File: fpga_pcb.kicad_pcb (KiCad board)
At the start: 2 copper layers, 254 parts, among them J1 USB_B_Mini, J10 Conn_02x08_Odd_Even, J11 Conn_02x08_Odd_Even, J12 5VIN, J13 Conn_01x10, J14 RJ45_Halo_HFJ11-x2450E-LxxRL, J2 Conn_01x06, J3 Conn_01x06, J4 Conn_01x06, J5 Conn_01x06, J6 Conn_01x06, J7 Conn_01x06, J8 Conn_01x06, J9 Conn_01x06, SW1 SW_Push, SW2 SW_Push, U10 LAN8720A, U2 23AA02M-IST, U3 TPS62A02APDDC, U4 TLV75733PDBV, U5 TPS2116DRL, U6 93AAxxBT-xOT, U7 USBLC6-2SC6, U8 FT4232H, U9 ADC1283, Y1 ECS-2520MV-500-xx, Y2 Crystal_GND24

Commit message: More layout
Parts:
- D7: footprint Diode_SMD:D_SOD-123 -> Diode_SMD:D_SMA
- D8: footprint Diode_SMD:D_SOD-923 -> Diode_SMD:D_SMA
- moved J9 302.0 mm to (258.0, 118.0), turned to -90 degrees
- moved J8 301.8 mm to (258.0, 106.0), turned to -90 degrees
- moved J7 301.7 mm to (258.0, 94.0), turned to -90 degrees
- moved J6 301.7 mm to (258.0, 82.0), turned to -90 degrees
- moved J5 291.2 mm to (244.0, 118.0), turned to -90 degrees
- moved J4 290.5 mm to (244.0, 106.0), turned to -90 degrees
- moved J3 290.0 mm to (244.0, 94.0), turned to -90 degrees
- moved J2 289.4 mm to (244.0, 82.0), turned to -90 degrees
- moved C54 289.0 mm to (253.5, 103.5), turned to -90 degrees
- moved C52 288.7 mm to (253.5, 79.5), turned to -90 degrees
- moved C53 288.7 mm to (253.5, 91.5), turned to -90 degrees
- moved C55 287.5 mm to (253.5, 115.5), turned to -90 degrees
- moved R61 281.4 mm to (254.0, 99.0)
- moved R62 281.3 mm to (254.0, 100.5), turned to 180 degrees
- moved R59 281.2 mm to (254.0, 87.0)
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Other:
- copper layers 2 -> 4
- board text added: "3V3 GND SCK D0 WS SEL"
- board text added: "3V3 GND SCK D1 WS SEL"
- board text added: "3V3 GND SCK D2 WS SEL"
- board text added: "3V3 GND SCK D3 WS SEL"

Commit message: More layout
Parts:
- moved J9 226.6 mm to (49.5, 206.8), turned to 180 degrees
- moved R66 224.8 mm to (43.0, 202.6), turned to 90 degrees
- moved R65 223.9 mm to (44.5, 202.6), turned to -90 degrees
- moved J8 220.8 mm to (61.5, 206.8), turned to 180 degrees
- moved C55 219.4 mm to (52.0, 202.2), turned to 180 degrees
- moved R64 218.5 mm to (55.0, 202.8), turned to 90 degrees
- moved R63 217.8 mm to (56.5, 202.8), turned to -90 degrees
- moved C2 217.6 mm to (55.2, 185.0), turned to -90 degrees
- moved J7 216.2 mm to (73.5, 206.8), turned to 180 degrees
- moved C1 214.7 mm to (74.5, 160.5), turned to 180 degrees
- moved C3 214.4 mm to (53.2, 185.0), turned to -90 degrees
- moved C54 213.7 mm to (64.0, 202.2), turned to 180 degrees
- moved C24 213.5 mm to (74.2, 174.8)
- moved R62 213.1 mm to (67.0, 202.8), turned to 90 degrees
- moved J6 212.9 mm to (85.5, 206.8), turned to 180 degrees
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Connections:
- J12 pad 1: Net-(D7-K) -> GND
- J12 pad 2: GND -> Net-(D7-K)
- U1 pad 2: /FPGA/UART.TX -> /FPGA/I2S.SCK
- U1 pad 29: /FPGA/BB0 -> /FPGA/USR_LED_R
- U1 pad 3: /FPGA/UART.RX -> /FPGA/I2S.WS
- U1 pad 30: /FPGA/BB1 -> /FPGA/USR_LED_G
- U1 pad 32: /FPGA/BB2 -> /FPGA/USR_LED_B
- U1 pad 33: /FPGA/BB3 -> /ADC/ADC_SPI.CS
- U1 pad 35: /FPGA/BB4 -> /ADC/ADC_SPI.SCLK
- U1 pad 36: /FPGA/BB5 -> /ADC/ADC_SPI.DIN
- U1 pad 37: /FPGA/BB6 -> /ADC/ADC_SPI.DOUT
- U1 pad 38: /FPGA/BB7 -> /FPGA/RAM.SIO0
- U1 pad 4: /FPGA/USR_LED_R -> /FPGA/I2S.DATA0
- U1 pad 40: /FPGA/I2S.SCK -> /FPGA/RAM.SCK
- U1 pad 41: /FPGA/I2S.WS -> /FPGA/RAM.SIO3
- U1 pad 43: /FPGA/I2S.DATA0 -> /FPGA/RAM.CS
- U1 pad 44: /FPGA/I2S.DATA1 -> /FPGA/RAM.SIO1
- U1 pad 46: /FPGA/I2S.DATA2 -> /FPGA/RAM.SIO2
- U1 pad 47: /FPGA/I2S.DATA3 -> /FPGA/GPIO0
- U1 pad 48: /FPGA/GPIO0 -> /FPGA/GPIO1
- U1 pad 49: /FPGA/GPIO1 -> /FPGA/GPIO2
- U1 pad 5: /FPGA/USR_LED_G -> /FPGA/I2S.DATA1
- U1 pad 51: /FPGA/GPIO2 -> /FPGA/GPIO3
- U1 pad 52: /FPGA/GPIO3 -> /FPGA/GPIO4
- U1 pad 54: /FPGA/GPIO4 -> /FPGA/GPIO5
- U1 pad 55: /FPGA/GPIO5 -> /FPGA/GPIO6
- U1 pad 56: /FPGA/GPIO6 -> /FPGA/GPIO7
- U1 pad 62: /FPGA/GPIO7 -> /FPGA/BB0
- U1 pad 63: /ADC/ADC_SPI.CS -> /FPGA/BB1
- U1 pad 65: /ADC/ADC_SPI.SCLK -> /FPGA/BB2
- U1 pad 66: /ADC/ADC_SPI.DIN -> /FPGA/BB3
- U1 pad 67: /ADC/ADC_SPI.DOUT -> /FPGA/BB4
- U1 pad 68: /FPGA/RAM.CS -> /FPGA/BB5
- U1 pad 7: /FPGA/CLK -> /FPGA/I2S.DATA2
- U1 pad 71: /FPGA/RAM.SCK -> /FPGA/BB6
- U1 pad 73: /FPGA/RAM.SIO0 -> /FPGA/BB7
- U1 pad 74: /FPGA/RAM.SIO1 -> /FPGA/UART.TX
- U1 pad 77: /FPGA/RAM.SIO2 -> /FPGA/UART.RX
- U1 pad 78: /FPGA/RAM.SIO3 -> /Ethernet/RMII.TXD0
- U1 pad 79: /Ethernet/RMII.TXD0 -> /Ethernet/RMII.TXD1
- U1 pad 80: /Ethernet/RMII.TXD1 -> /Ethernet/RMII.TXEN
- U1 pad 85: /Ethernet/RMII.TXEN -> /Ethernet/RMII.RXD0
- U1 pad 86: /Ethernet/RMII.RXD0 -> /FPGA/CLK
- U1 pad 9: /FPGA/USR_LED_B -> /FPGA/I2S.DATA3
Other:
- board outline added: 100 x 65 mm
- board text added: "3V3 GND IO0 IO1 IO2 IO3 IO4 IO5 IO6 IO7"
- board text added: "GND 3V3 HOLD RSTN CS MISO MOSI SCLK"
- board text added: "GND 3V3 TMS TDO TDI TCK RX TX"

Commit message: Initial layout
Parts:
- moved R17 209.8 mm to (84.0, 160.2), turned to 90 degrees
- moved R8 208.5 mm to (51.8, 185.5), turned to 90 degrees
- moved R12 205.4 mm to (59.8, 185.5), turned to 90 degrees
- moved R15 201.8 mm to (87.0, 160.2), turned to -90 degrees
- moved D1 201.1 mm to (80.2, 157.2), turned to -90 degrees
- moved R21 199.1 mm to (78.8, 160.2), turned to 90 degrees
- moved R16 199.1 mm to (85.5, 160.2), turned to -90 degrees
- moved D2 198.4 mm to (78.8, 157.2), turned to -90 degrees
- moved R14 198.2 mm to (80.2, 160.2), turned to 90 degrees
- moved R25 197.2 mm to (66.0, 180.2)
- moved R7 193.5 mm to (58.8, 158.0), turned to 90 degrees
- moved R18 192.5 mm to (60.2, 161.5), turned to -90 degrees
- moved R19 191.6 mm to (61.8, 161.5), turned to -90 degrees
- moved R27 191.0 mm to (37.8, 176.8), turned to 180 degrees
- moved R10 190.3 mm to (65.2, 155.0), turned to 180 degrees
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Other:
- board text added: "A7 A6 A5 A4 A3 A2 A1 A0"

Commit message: Routing done
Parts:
- removed JP1: SolderJumper_2_Bridged, Jumper:SolderJumper-2_P1.3mm_Bridged_RoundedPad1.0x1.5mm
- removed JP2: SolderJumper_2_Open, Jumper:SolderJumper-2_P1.3mm_Open_RoundedPad1.0x1.5mm
- removed TP15, TP16, TP17, TP19, TP20, TP21, TP22, TP23, TP24, TP25, TP26, TP27, TP28, TP35, TP36, TP37, TP38, TP39, TP4, TP40, TP41, TP42, TP43, TP44, TP45, TP5, TP6, TP7, TP8, TP9: TestPoint, TestPoint:TestPoint_Pad_D1.0mm
- added NT1: NetTie_2, NetTie:NetTie-2_SMD_Pad0.5mm, F.Cu at (31.7, 195.4)
- added R45: 5.1k, Resistor_SMD:R_0603_1608Metric, F.Cu at (10.2, 156.5)
- added R46: 5.1k, Resistor_SMD:R_0603_1608Metric, F.Cu at (10.2, 163.5)
- J1: value USB_B_Mini -> USB_C_Receptacle_USB2.0_16P; footprint Connector_USB:USB_Mini-B_Wuerth_65100516121_Horizontal -> Connector_USB:USB_C_Receptacle_GCT_USB4105-xx-A_16P_TopMnt_Horizontal
- moved TP29 121.0 mm to (85.5, 187.5)
- moved TP2 119.0 mm to (73.6, 182.5)
- moved TP33 115.3 mm to (83.5, 187.5)
- moved TP1 113.3 mm to (80.2, 152.1)
- moved TP30 110.2 mm to (73.0, 187.8)
- moved TP32 100.7 mm to (61.5, 187.5)
- moved TP3 95.2 mm to (34.2, 195.2)
- moved TP31 93.3 mm to (46.5, 185.5)
- moved TP34 92.0 mm to (48.8, 187.5)
- moved TP10 72.0 mm to (24.2, 181.0)
- moved TP11 67.6 mm to (33.2, 169.8)
- moved TP12 63.3 mm to (9.50, 168.8)
- moved TP13 59.1 mm to (24.0, 166.5)
- moved TP18 50.2 mm to (40.2, 154.0)
- moved TP14 38.9 mm to (24.8, 148.0)
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- renumbered R45 to R47, R46 to R48, R47 to R49, R48 to R50, R49 to R89, R50 to R90
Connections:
- F1 pad 2: Net-(J1-VBUS) -> Net-(F1-Pad2)
- J1 pad SH: Net-(J1-Shield) -> GND
- U1 pad 100: /Ethernet/RMII.INT -> /Ethernet/RMII.RXD1
- U1 pad 4: /FPGA/I2S.DATA0 -> /FPGA/I2S.DATA3
- U1 pad 5: /FPGA/I2S.DATA1 -> /FPGA/I2S.DATA2
- U1 pad 7: /FPGA/I2S.DATA2 -> /FPGA/I2S.DATA1
- U1 pad 74: /FPGA/UART.TX -> /FPGA/UART.RX
- U1 pad 77: /FPGA/UART.RX -> /FPGA/UART.TX
- U1 pad 78: /Ethernet/RMII.TXD0 -> /Ethernet/RMII.TXD1
- U1 pad 79: /Ethernet/RMII.TXD1 -> /Ethernet/RMII.TXD0
- U1 pad 85: /Ethernet/RMII.RXD0 -> /Ethernet/RMII.RSTN
- U1 pad 87: /Ethernet/RMII.RXD1 -> /Ethernet/RMII.INT
- U1 pad 89: /Ethernet/RMII.RXER -> /Ethernet/RMII.MDC
- U1 pad 9: /FPGA/I2S.DATA3 -> /FPGA/I2S.DATA0
- U1 pad 94: /Ethernet/RMII.CRS_DV -> /Ethernet/RMII.MDIO
- U1 pad 95: /Ethernet/RMII.MDIO -> /Ethernet/RMII.CRS_DV
- U1 pad 98: /Ethernet/RMII.MDC -> /Ethernet/RMII.RXER
- U1 pad 99: /Ethernet/RMII.RSTN -> /Ethernet/RMII.RXD0
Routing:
- net GND: track 0.00 -> 185.2 mm, vias 0 -> 103
- net +3.3V: track 0.00 -> 157.7 mm, vias 0 -> 64
- net /FPGA/I2S.SCK: track 0.00 -> 105.1 mm, vias 0 -> 6
- net /FPGA/I2S.WS: track 0.00 -> 102.5 mm, vias 0 -> 4
- net /FPGA/FT.RESETN: track 0.00 -> 93.5 mm, vias 0 -> 5
- net /FPGA/FT.CS: track 0.00 -> 83.7 mm, vias 0 -> 6
- net /FPGA/FT.SCLK: track 0.00 -> 81.3 mm, vias 0 -> 3
- net /FPGA/FT.MOSI: track 0.00 -> 78.1 mm, vias 0 -> 3
- net /FPGA/FT.MISO: track 0.00 -> 78.0 mm, vias 0 -> 3
- net /FPGA/FT.HOLD: track 0.00 -> 70.1 mm, vias 0 -> 4
- net /FPGA/JTAG.TMS: track 0.00 -> 63.3 mm, vias 0 -> 4
- net /FPGA/JTAG.TDO: track 0.00 -> 62.8 mm, vias 0 -> 4
- net /FPGA/JTAG.TDI: track 0.00 -> 61.5 mm, vias 0 -> 4
- net /FPGA/JTAG.TCK: track 0.00 -> 60.3 mm, vias 0 -> 4
- net /FPGA/I2S.DATA0: track 0.00 -> 54.8 mm, vias 0 -> 2
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- added copper zone on F.Cu, net +1V2
- added copper zone on In2.Cu, net +1V2
- added copper zone on In2.Cu, net +3.3V
- added copper zone on F.Cu, net GND
- added copper zone on In1.Cu, net GND
- added copper zone on F.Cu, net Net-(D7-K)
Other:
- board text added: "1V2"
- board text added: "1V8"
- board text added: "3V3"
- board text added: "3V3 ERR DNE"
- board text added: "5V"
- board text added: "5V VB"
- board text added: "CDONE"
- board text added: "CLK"
- board text added: "C_RSTN"
- board text added: "D0"
- board text added: "D1"
- board text added: "D2"
- board text added: "D3"
- board text added: "EEDO"
- board text added: "PL_RSTN"
- board text added: "SCK"
- board text added: "VUSB"
- board text added: "WS"

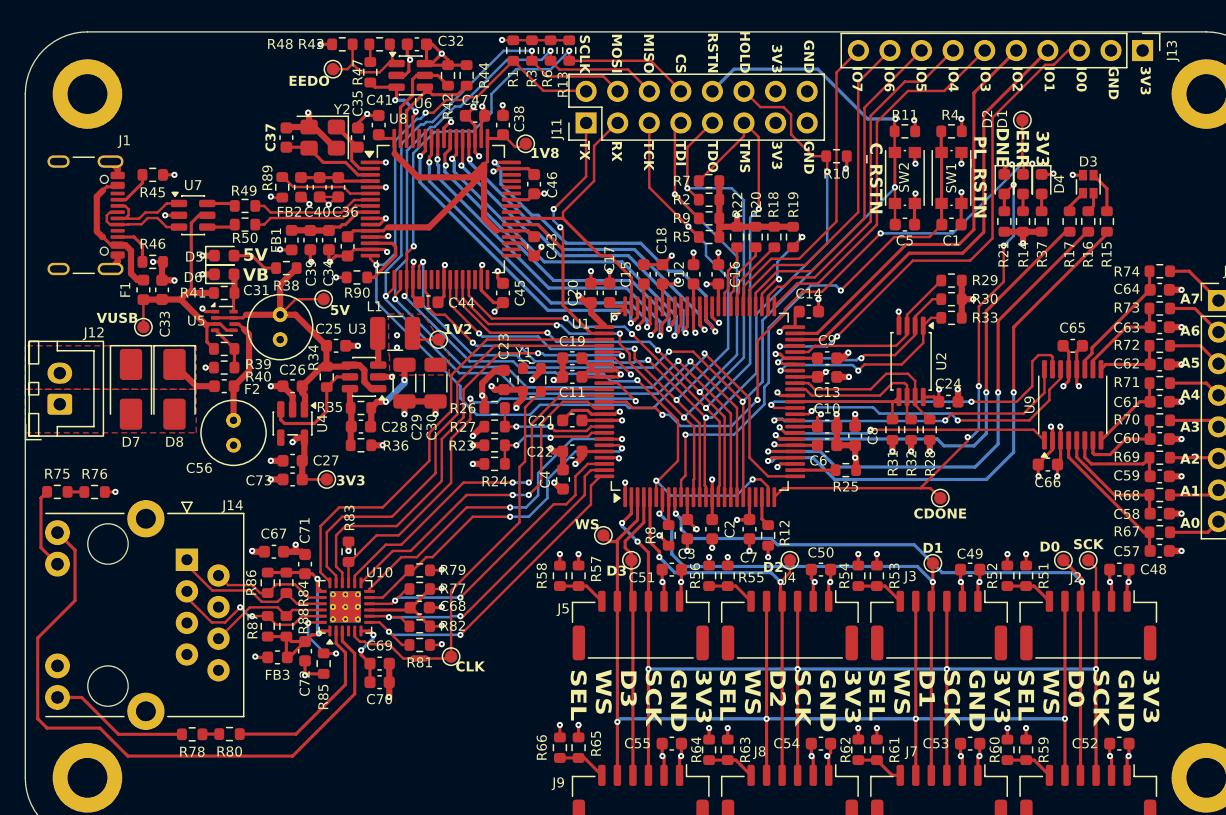
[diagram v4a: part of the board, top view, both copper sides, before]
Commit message: Added SPI bus buffer
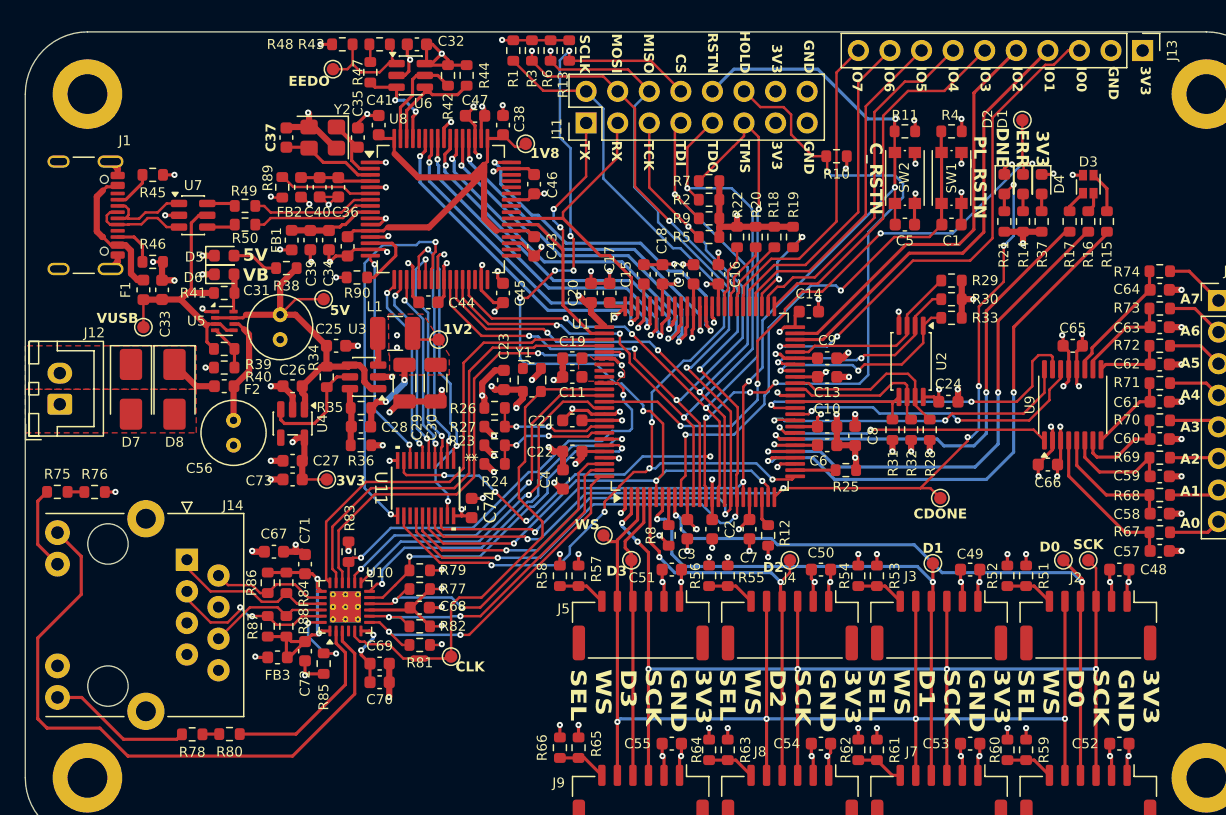
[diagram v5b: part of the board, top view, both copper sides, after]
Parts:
- added C74: 100nF, Capacitor_SMD:C_0603_1608Metric, F.Cu at (35.9, 183.3)
- added U11: SN74LV244AQDGSRQ1, SN74LV244AQDGSRQ1:VSSOP20_DGS_TEX, F.Cu at (32.2, 181.7)
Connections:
- net /FPGA/CDONE renamed /FPGA/FT.CDONE
- U8 pad 16: /FPGA/FT.SCLK -> /USB/FT_SCLK
- U8 pad 17: /FPGA/FT.MOSI -> /USB/FT_MOSI
- U8 pad 18: /FPGA/FT.MISO -> /USB/FT_MISO
- U8 pad 19: /FPGA/FT.CS -> /USB/FT_SS
- U8 pad 21: /FPGA/FT.RESETN -> /USB/FT_RSTN
- U8 pad 22: /FPGA/FT.HOLD -> /USB/FT_CDONE
- U8 pad 23: unconnected-(U8-ADBUS6-Pad23) -> /USB/FT_HOLD
- U8 pad 24: unconnected-(U8-ADBUS7-Pad24) -> /USB/FT_ENA
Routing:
- net /USB/FT_HOLD: track 0.00 -> 31.2 mm, vias 0 -> 2
- net /FPGA/FT.CDONE: track 44.1 -> 75.2 mm, vias 4 -> 6
- net /USB/FT_ENA: track 0.00 -> 26.9 mm, vias 0 -> 3
- net /USB/FT_RSTN: track 0.00 -> 20.6 mm, vias 0 -> 2
- net /USB/FT_CDONE: track 0.00 -> 19.1 mm, vias 0 -> 2
- net /USB/FT_SCLK: track 0.00 -> 17.8 mm, vias 0 -> 2
- net /USB/FT_MOSI: track 0.00 -> 16.0 mm, vias 0 -> 2
- net +1V2: track 52.6 -> 36.6 mm
- net /USB/FT_MISO: track 0.00 -> 15.9 mm, vias 0 -> 2
- net /USB/FT_SS: track 0.00 -> 15.7 mm, vias 0 -> 2
- net /FPGA/FT.HOLD: track 70.1 -> 84.9 mm, vias 4 -> 8
- net /FPGA/FT.CS: track 83.7 -> 92.1 mm, vias 6 -> 9
- net /FPGA/FT.RESETN: track 93.5 -> 85.5 mm
- net +3.3V: track 157.7 -> 161.1 mm, vias 64 -> 66
- net /FPGA/CLK: track 31.7 -> 34.4 mm
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
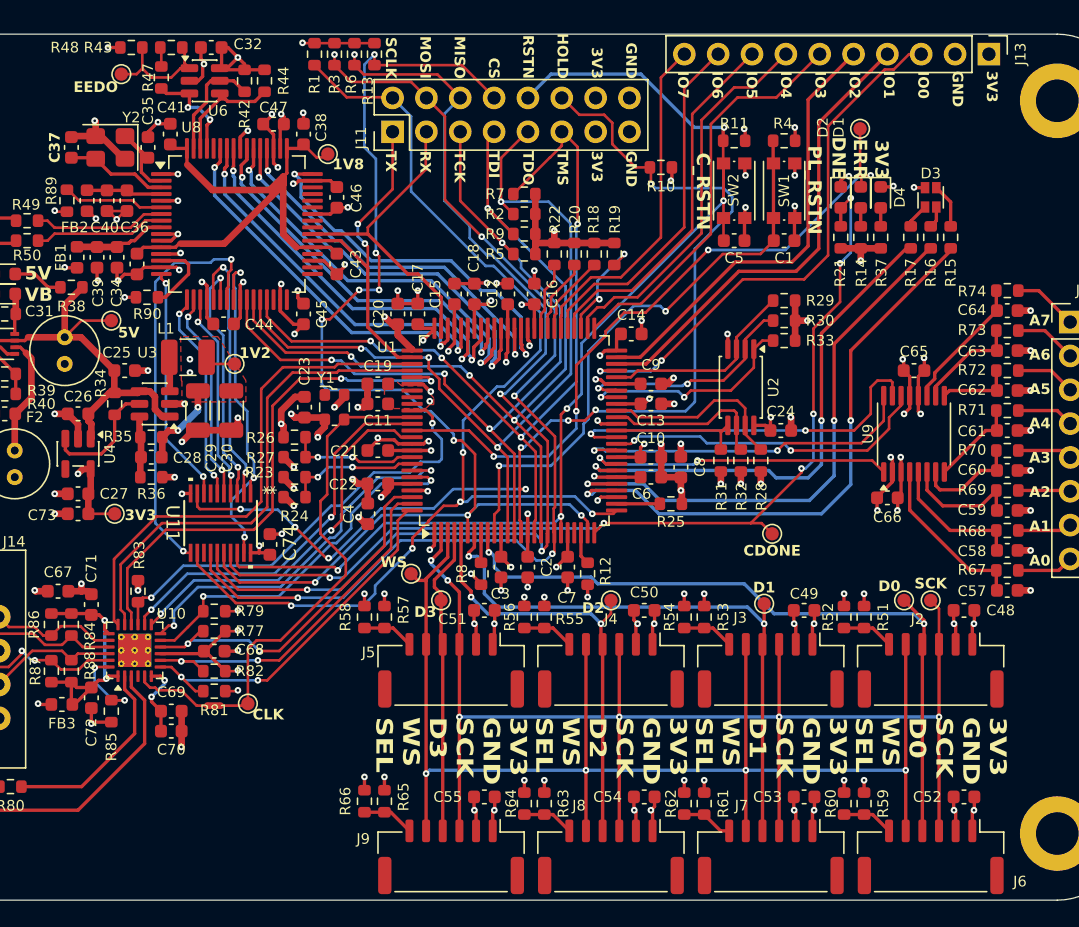
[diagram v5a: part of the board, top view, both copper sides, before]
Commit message: Added decal and gerbers
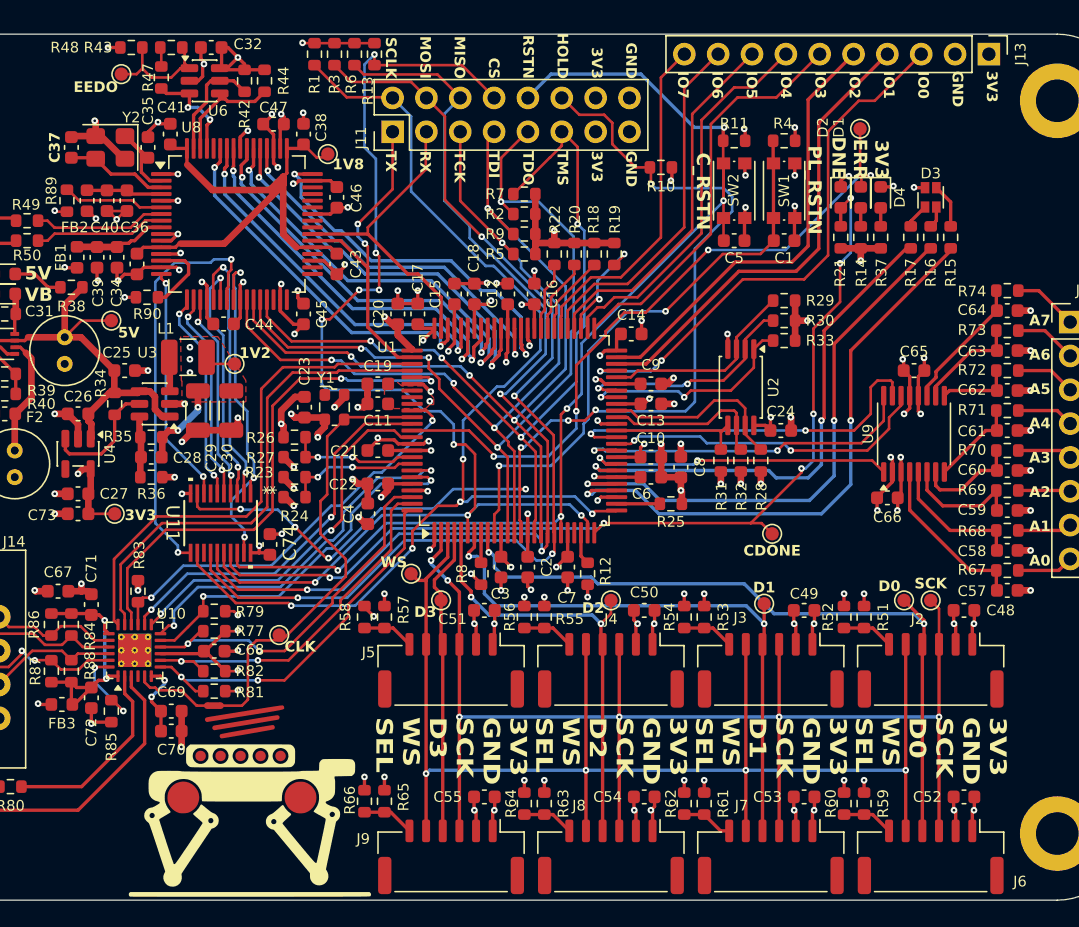
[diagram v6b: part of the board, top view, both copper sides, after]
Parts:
- added G*** (x3): LOGO, LOGO, F.Cu at (34.4, 202.8)
- moved TP3 5.66 mm to (36.6, 190.1)
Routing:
- net /Ethernet/RMII.RSTN: track 34.1 -> 31.5 mm
- net /FPGA/FT.MOSI: track 80.0 -> 78.9 mm, vias 5 -> 4
- net /FPGA/FT.MISO: track 79.9 -> 79.1 mm, vias 4 -> 3
- net /Ethernet/RMII.RXD1: track 28.0 -> 28.7 mm
- net /FPGA/FT.CS: track 92.1 -> 92.7 mm
- net +1V2: vias 13 -> 14

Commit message: Finalized
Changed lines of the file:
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@@
 	)
 	(segment
-		(start 27.3 181.7)
-		(end 27.3 163.6)
+		(start 31.45 162.15)
+		(end 31.7 161.9)
 		(width 0.2)
 		(layer "B.Cu")
@@
 	)
 	(segment
-		(start 28.75 162.15)
-		(end 31.45 162.15)
-		(width 0.2)
-		(layer "B.Cu")
-		(net "/USB/FT_HOLD")
-	)
-	(segment
-		(start 27.3 163.6)
-		(end 28.75 162.15)
+		(start 27.3 163.2)
+		(end 28.35 162.15)
 		(width 0.2)
 		(layer "B.Cu")
@@
 	)
 	(segment
-		(start 29 183.4)
-		(end 27.3 181.7)
+		(start 28.35 162.15)
+		(end 31.45 162.15)
 		(width 0.2)
 		(layer "B.Cu")
@@
 	)
 	(segment
-		(start 31.45 162.15)
-		(end 31.7 161.9)
+		(start 27.3 181.7)
+		(end 27.3 163.2)
 		(width 0.2)
 		(layer "B.Cu")
+		(net "/USB/FT_HOLD")
+	)
+	(segment
+		(start 29 183.4)
+		(end 27.3 181.7)
+		(width 0.2)
+		(layer "B.Cu")
